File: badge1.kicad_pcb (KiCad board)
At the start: 2 copper layers, 50 x 100 mm, 23 parts, among them P1 CONN_01X04, P2 USB_A, P3 CONN_01X04, P4 CONN_01X03, SW1 SW_PUSH, U1 MCP1700-3302E/TO, U2 custom_logo, U3 Hillhacks_logo, U4 proto_area, U5 badge_hole2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

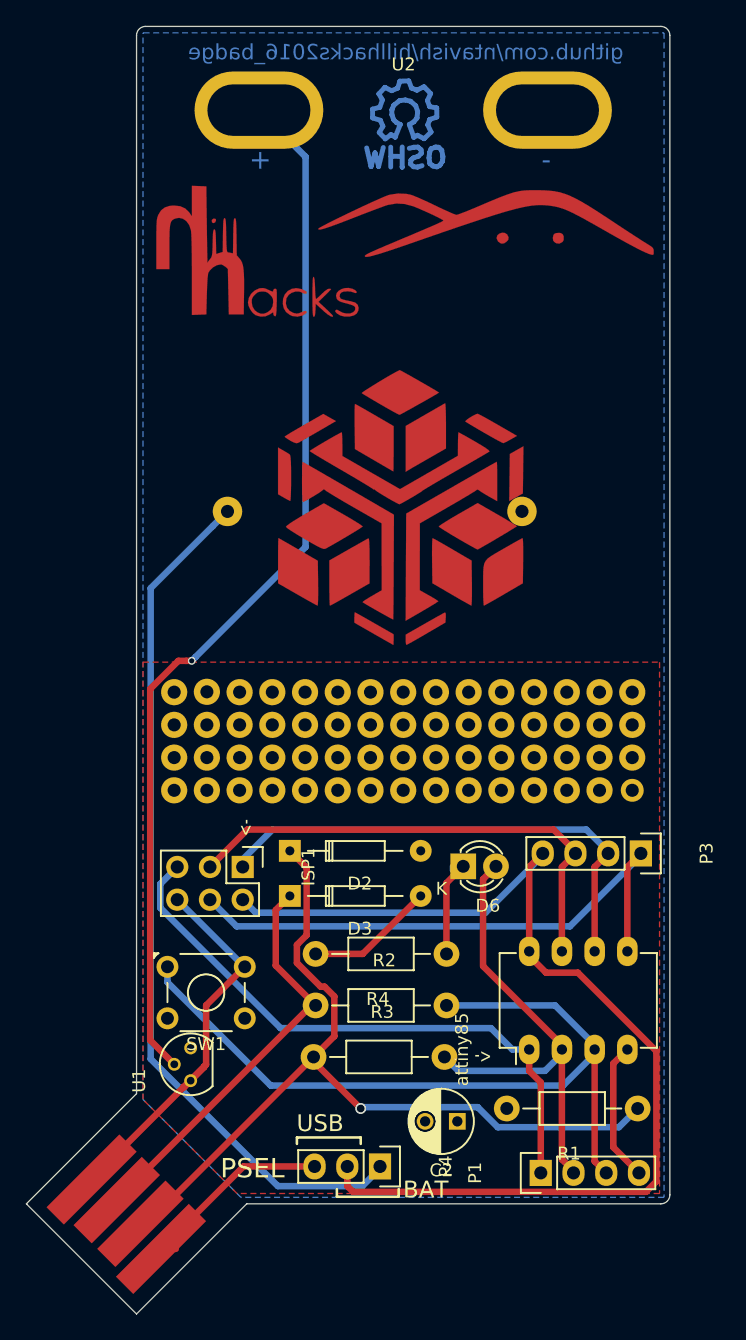
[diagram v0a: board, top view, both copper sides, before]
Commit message: fixed positions of silkscreen texts, tesseract logo to F.Mask
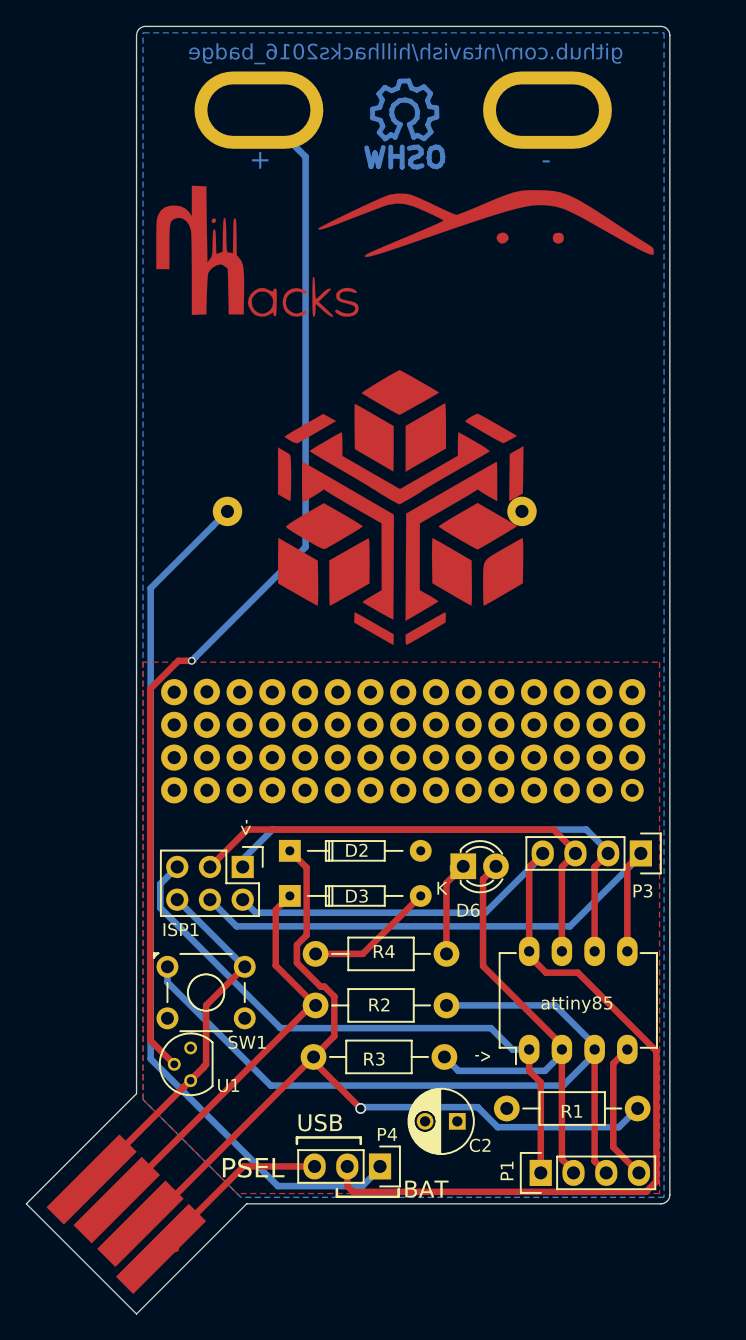
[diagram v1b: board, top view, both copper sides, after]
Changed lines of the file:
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@@
     (descr SW_TH_Tactile_Omron_B3F-10xx)
     (tags "Omron B3F-10xx")
-    (fp_text reference SW1 (at 3 6) (layer F.SilkS)
+    (fp_text reference SW1 (at 6.2 5.9) (layer F.SilkS)
       (effects (font (size 1 1) (thickness 0.15)))
     )
@@
     (descr "Symbol, OSHW-Logo, Copper Top,")
     (tags "Symbol, OSHW-Logo, Copper Top,")
-    (fp_text reference U2 (at 0.572764 -4 180) (layer F.SilkS)
+    (fp_text reference U2 (at 0.572764 -4) (layer F.SilkS) hide
       (effects (font (size 1 1) (thickness 0.15)))
     )
@@
       (effects (font (size 1 1) (thickness 0.15)) (justify mirror))
     )
-    (fp_text value Battery (at 0 -12.7 180) (layer B.Fab)
+    (fp_text value Battery (at -12.65 -8.2 180) (layer B.Fab) hide
       (effects (font (size 1 1) (thickness 0.15)) (justify mirror))
     )
@@
     (descr "Through hole pin header")
     (tags "pin header")
-    (fp_text reference ISP1 (at 0 -5.1 270) (layer F.SilkS)
+    (fp_text reference ISP1 (at 4.9 4.79 360) (layer F.SilkS)
       (effects (font (size 1 1) (thickness 0.15)))
     )
@@
     (descr "Through hole pin header")
     (tags "pin header")
-    (fp_text reference P1 (at 0 -5.1 90) (layer F.SilkS)
+    (fp_text reference P1 (at 0.15 -2.58 90) (layer F.SilkS)
       (effects (font (size 1 1) (thickness 0.15)))
     )
@@
     (descr "Through hole pin header")
     (tags "pin header")
-    (fp_text reference P3 (at 0 -5.1 270) (layer F.SilkS)
+    (fp_text reference P3 (at 2.95 -0.15 360) (layer F.SilkS)
       (effects (font (size 1 1) (thickness 0.15)))
     )
@@
     (descr "8-lead dip package, row spacing 7.62 mm (300 mils), longer pads")
     (tags "dil dip 2.54 300")
-    (fp_text reference attiny85 (at 0 -5.22 90) (layer F.SilkS)
+    (fp_text reference attiny85 (at 3.57 3.72 180) (layer F.SilkS)
       (effects (font (size 1 1) (thickness 0.15)))
     )
@@
     (descr "Radial Electrolytic Capacitor Diameter 5mm x Length 11mm, Pitch 2.5mm")
     (tags "Electrolytic Capacitor")
-    (fp_text reference C2 (at 1.25 -3.8 180) (layer F.SilkS)
+    (fp_text reference C2 (at -1.8 -1.9 180) (layer F.SilkS)
       (effects (font (size 1 1) (thickness 0.15)))
     )
@@
     (descr "Diode, DO-35,  SOD27, Horizontal, RM 10mm")
     (tags "Diode, DO-35, SOD27, Horizontal, RM 10mm, 1N4148,")
-    (fp_text reference D2 (at 5.43052 2.53746) (layer F.SilkS)
+    (fp_text reference D2 (at 5.20052 -0.00254) (layer F.SilkS)
       (effects (font (size 1 1) (thickness 0.15)))
     )
@@
     (descr "Diode, DO-35,  SOD27, Horizontal, RM 10mm")
     (tags "Diode, DO-35, SOD27, Horizontal, RM 10mm, 1N4148,")
-    (fp_text reference D3 (at 5.43052 2.53746) (layer F.SilkS)
+    (fp_text reference D3 (at 5.20052 0.04746) (layer F.SilkS)
       (effects (font (size 1 1) (thickness 0.15)))
     )
@@
     (descr "LED 3mm round vertical")
     (tags "LED  3mm round vertical")
-    (fp_text reference D6 (at 1.91 3.06) (layer F.SilkS)
+    (fp_text reference D6 (at 0.39 3.45) (layer F.SilkS)
       (effects (font (size 1 1) (thickness 0.15)))
     )
@@
     (descr "Resistor, Axial,  RM 10mm, 1/3W")
     (tags "Resistor Axial RM 10mm 1/3W")
-    (fp_text reference R2 (at 5.32892 -3.50012) (layer F.SilkS)
+    (fp_text reference R2 (at 4.95 0) (layer F.SilkS)
       (effects (font (size 1 1) (thickness 0.15)))
     )
@@
     (descr "Resistor, Axial,  RM 10mm, 1/3W")
     (tags "Resistor Axial RM 10mm 1/3W")
-    (fp_text reference R3 (at 5.32892 -3.50012) (layer F.SilkS)
+    (fp_text reference R3 (at 4.71 0.2) (layer F.SilkS)
       (effects (font (size 1 1) (thickness 0.15)))
     )
@@
     (descr "Resistor, Axial,  RM 10mm, 1/3W")
     (tags "Resistor Axial RM 10mm 1/3W")
-    (fp_text reference R4 (at 5.32892 -3.50012 180) (layer F.SilkS)
+    (fp_text reference R4 (at 4.86 0.15 180) (layer F.SilkS)
       (effects (font (size 1 1) (thickness 0.15)))
     )
@@
     (descr "Through hole pin header")
     (tags "pin header")
-    (fp_text reference P4 (at 0 -5.1 270) (layer F.SilkS)
+    (fp_text reference P4 (at -2.45 -0.55 360) (layer F.SilkS)
       (effects (font (size 1 1) (thickness 0.15)))
     )
@@
     (descr "Resistor, Axial,  RM 10mm, 1/3W")
     (tags "Resistor Axial RM 10mm 1/3W")
-    (fp_text reference R1 (at 5.32892 -3.50012 180) (layer F.SilkS)
+    (fp_text reference R1 (at 5.1 -0.25 180) (layer F.SilkS)
       (effects (font (size 1 1) (thickness 0.15)))
     )
@@
     (descr "TO-92 leads molded, narrow, drill 0.6mm (see NXP sot054_po.pdf)")
     (tags "to-92 sc-43 sc-43a sot54 PA33 transistor")
-    (fp_text reference U1 (at 0 -4 90) (layer F.SilkS)
+    (fp_text reference U1 (at -0.41 2.95 180) (layer F.SilkS)
       (effects (font (size 1 1) (thickness 0.15)))
     )
@@
   (segment (start 161.62 111.8) (end 161.62 105.25) (width 0.508) (layer F.Cu) (net 13) (status 10))
   (segment (start 161.62 105.25) (end 162.67 104.2) (width 0.508) (layer F.Cu) (net 13) (status 20))
+  (segment (start 133.182907 88.950686) (end 132.882908 89.250685) (width 0.508) (layer B.Cu) (net 14))
   (segment (start 138.1 46.5) (end 141.722897 50.122897) (width 0.508) (layer B.Cu) (net 14))
+  (segment (start 141.722897 80.410696) (end 133.182907 88.950686) (width 0.508) (layer B.Cu) (net 14))
   (segment (start 141.722897 50.122897) (end 141.722897 80.410696) (width 0.508) (layer B.Cu) (net 14))
-  (segment (start 141.722897 80.410696) (end 133.182907 88.950686) (width 0.508) (layer B.Cu) (net 14))
-  (segment (start 133.182907 88.950686) (end 132.882908 89.250685) (width 0.508) (layer B.Cu) (net 14))
   (segment (start 132.458644 89.250685) (end 132.882908 89.250685) (width 0.508) (layer F.Cu) (net 14))
   (segment (start 131.843154 89.250685) (end 132.458644 89.250685) (width 0.508) (layer F.Cu) (net 14))
@@
       )
     )
+  )
+  (zone (net 0) (net_name "") (layer B.Cu) (hatch edge 0.508)
+    (connect_pads (clearance 0.508))
+    (min_thickness 0.254)
+    (keepout (tracks not_allowed) (vias not_allowed) (copperpour allowed))
+    (fill yes (arc_segments 16) (thermal_gap 0.508) (thermal_bridge_width 0.508))
+    (polygon
+      (pts
+        (xy 139.4 51.35) (xy 136.85 51.35) (xy 136.85 49.65) (xy 139.65 49.65) (xy 139.65 51.35)
+      )
+    )
+  )
+  (zone (net 0) (net_name "") (layer B.Cu) (hatch edge 0.508)
+    (connect_pads (clearance 0.508))
+    (min_thickness 0.254)
+    (keepout (tracks not_allowed) (vias not_allowed) (copperpour allowed))
+    (fill yes (arc_segments 16) (thermal_gap 0.508) (thermal_bridge_width 0.508))
+    (polygon
+      (pts
+        (xy 161.7 51.4) (xy 159.15 51.4) (xy 159.15 49.7) (xy 161.95 49.7) (xy 161.95 51.4)
+      )
+    )

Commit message: minor changes. increase via size. update rendering with colour.
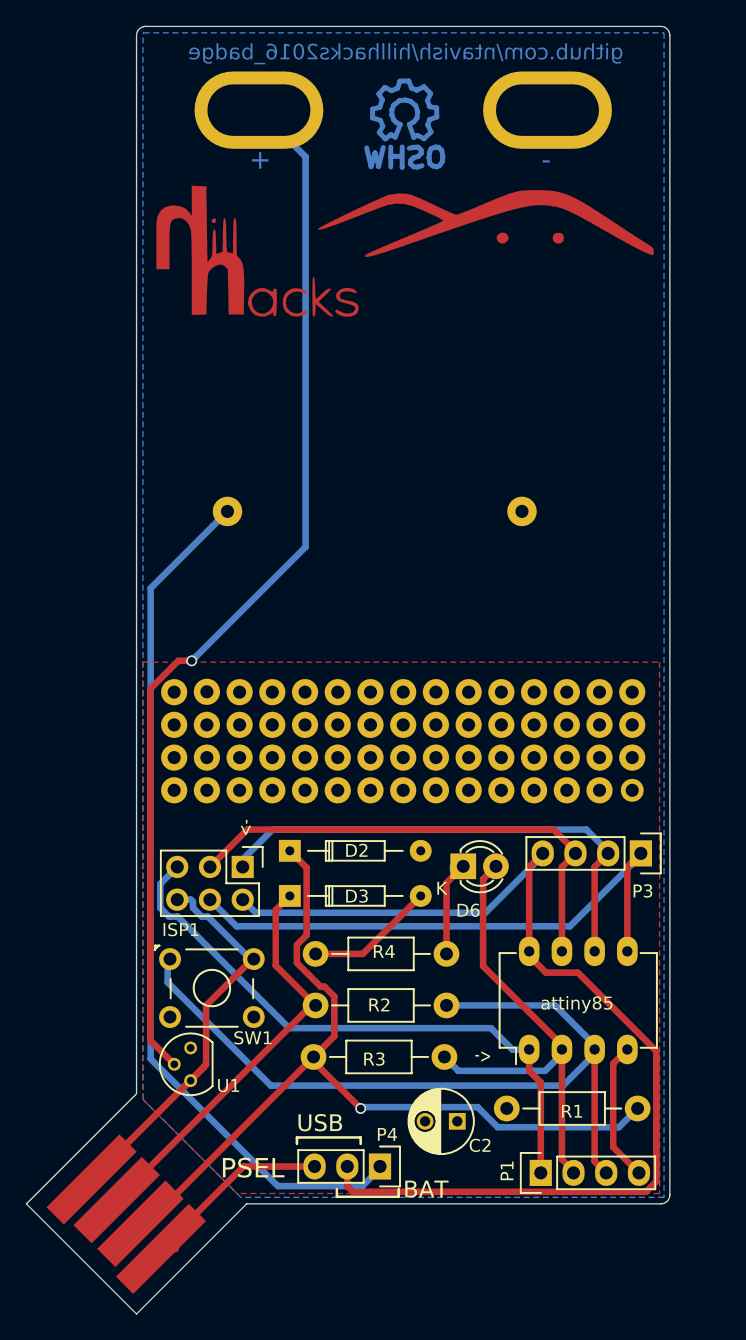
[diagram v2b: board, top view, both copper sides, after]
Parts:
- SW1: footprint Buttons_Switches_ThroughHole:SW_TH_Tactile_Omron_B3F-10xx -> badge_mod:OPL_DIP_BUTTON_TS-1109_BEST_SHENZEN
- moved SW1 0.57 mm to (131.4, 112.7)
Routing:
- net GND: track 52.5 -> 54.0 mm

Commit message: fixed mistakes and made button the reset button. added more legend.
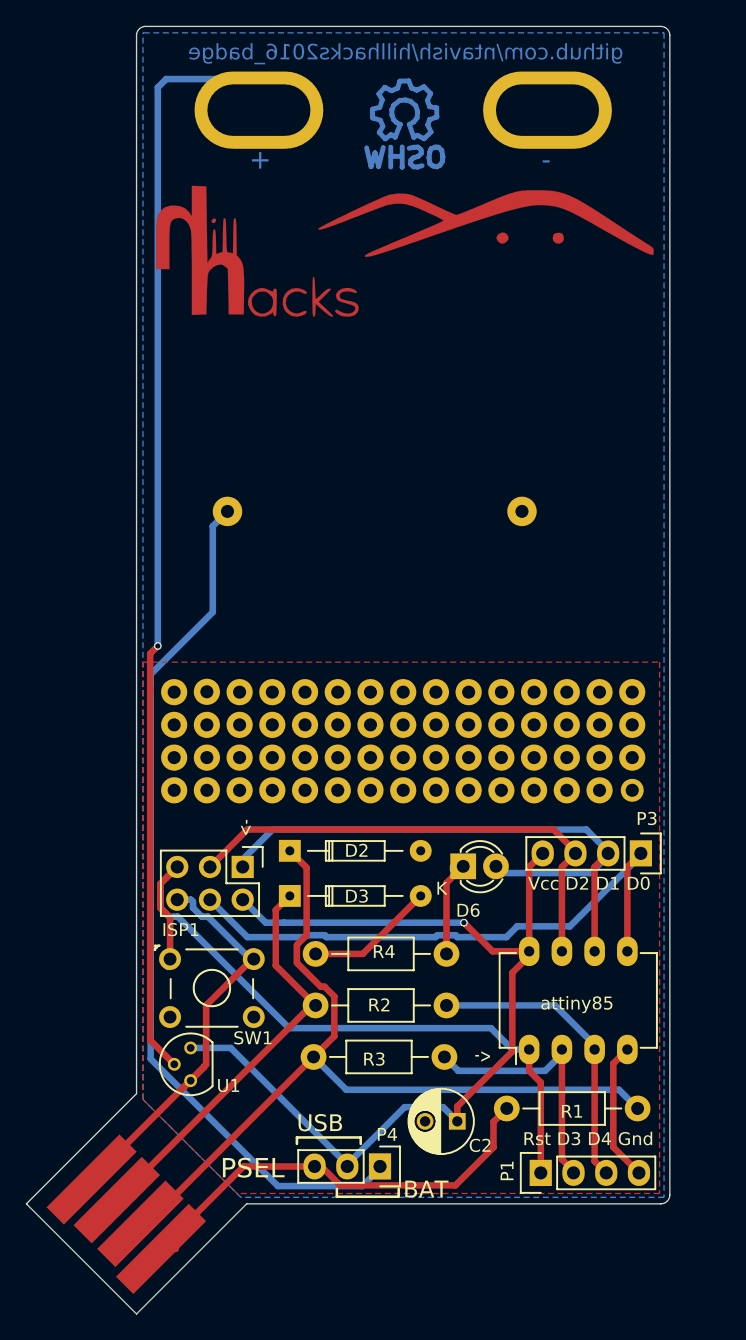
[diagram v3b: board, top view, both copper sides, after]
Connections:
- D6 pad 2: /D3 -> /D1
- R1 pad 2: VCC -> /VBUS
- SW1 pad 1: /D4 -> /RST
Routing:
- net /D4: track 62.5 -> 23.8 mm
- net /VBUS: track 15.7 -> 34.9 mm
- net /D3: track 38.2 -> 21.6 mm
- net /D1: track 38.8 -> 48.5 mm
- net VCC: track 84.1 -> 74.9 mm, vias 0 -> 1
- net /RST: track 47.2 -> 55.2 mm
- net /V_sec_bat: track 84.6 -> 88.6 mm
- net /USB-D-: track 66.0 -> 64.9 mm, vias 1 -> 0
- net /D0: track 45.3 -> 46.2 mm
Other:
- board text added: "Rst D3 D4 Gnd"
- board text added: "Vcc D2 D1 D0"

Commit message: Update schematic/layout with fixes. Update readme for small howto.
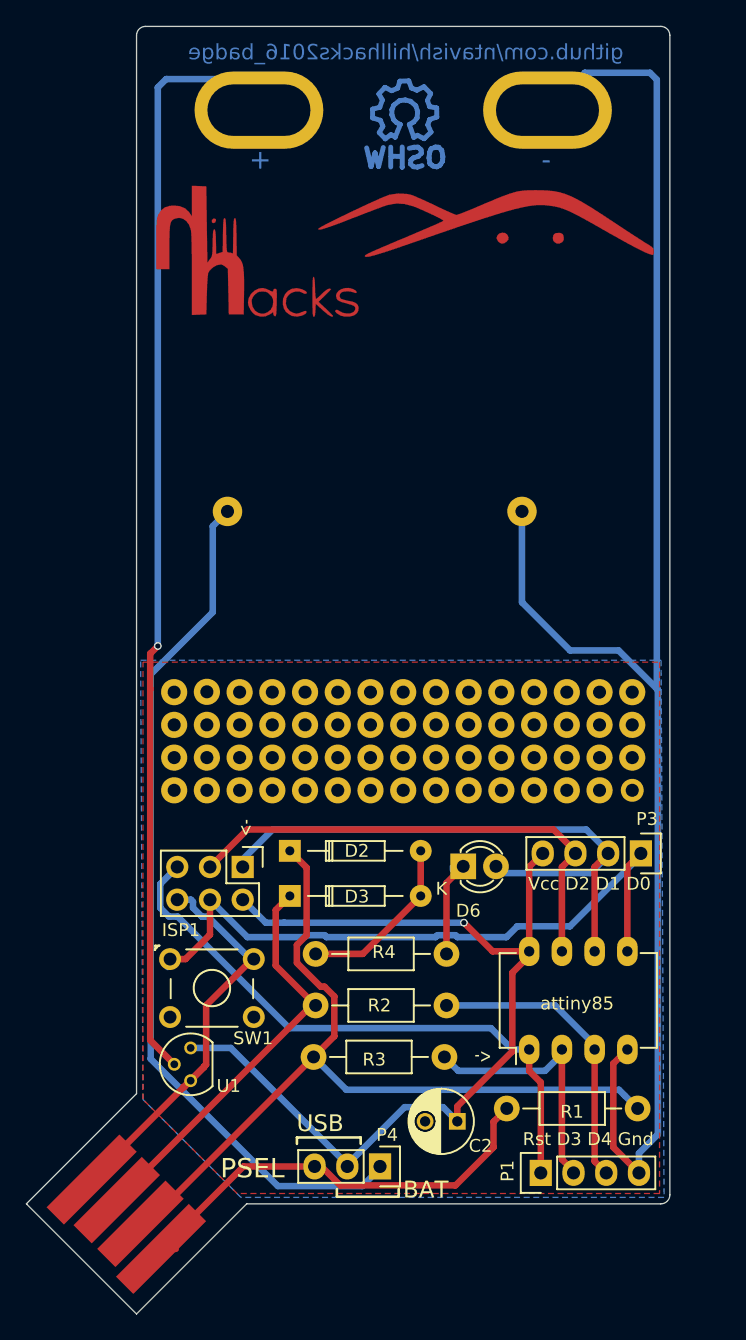
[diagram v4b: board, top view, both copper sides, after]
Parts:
- added U8: custom_logo, badge_mod:tesseract, B.Cu at (148.9, 77.3)
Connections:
- SW1 pad 1: /RST -> /D0
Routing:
- net GND: track 54.0 -> 173.5 mm
- net /RST: track 55.2 -> 47.2 mm
- net /D0: track 46.2 -> 52.8 mm
